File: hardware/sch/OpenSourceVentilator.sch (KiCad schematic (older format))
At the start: 16 parts, among them J101 Conn_TM1638_Disp, J102 24V Barrel Jack, J103 Conn_Stepper_Motor, J104 Conn_Beeper, J105 Conn_A4988_Stepper, J106 Conn_Motor_PWR, J107 Conn_Nano_PWR, J108 Conn_Nano_Pwr, J109 Conn_BME280, J110 Conn_A4988_Stepper, J111 Conn_Motor_PWR

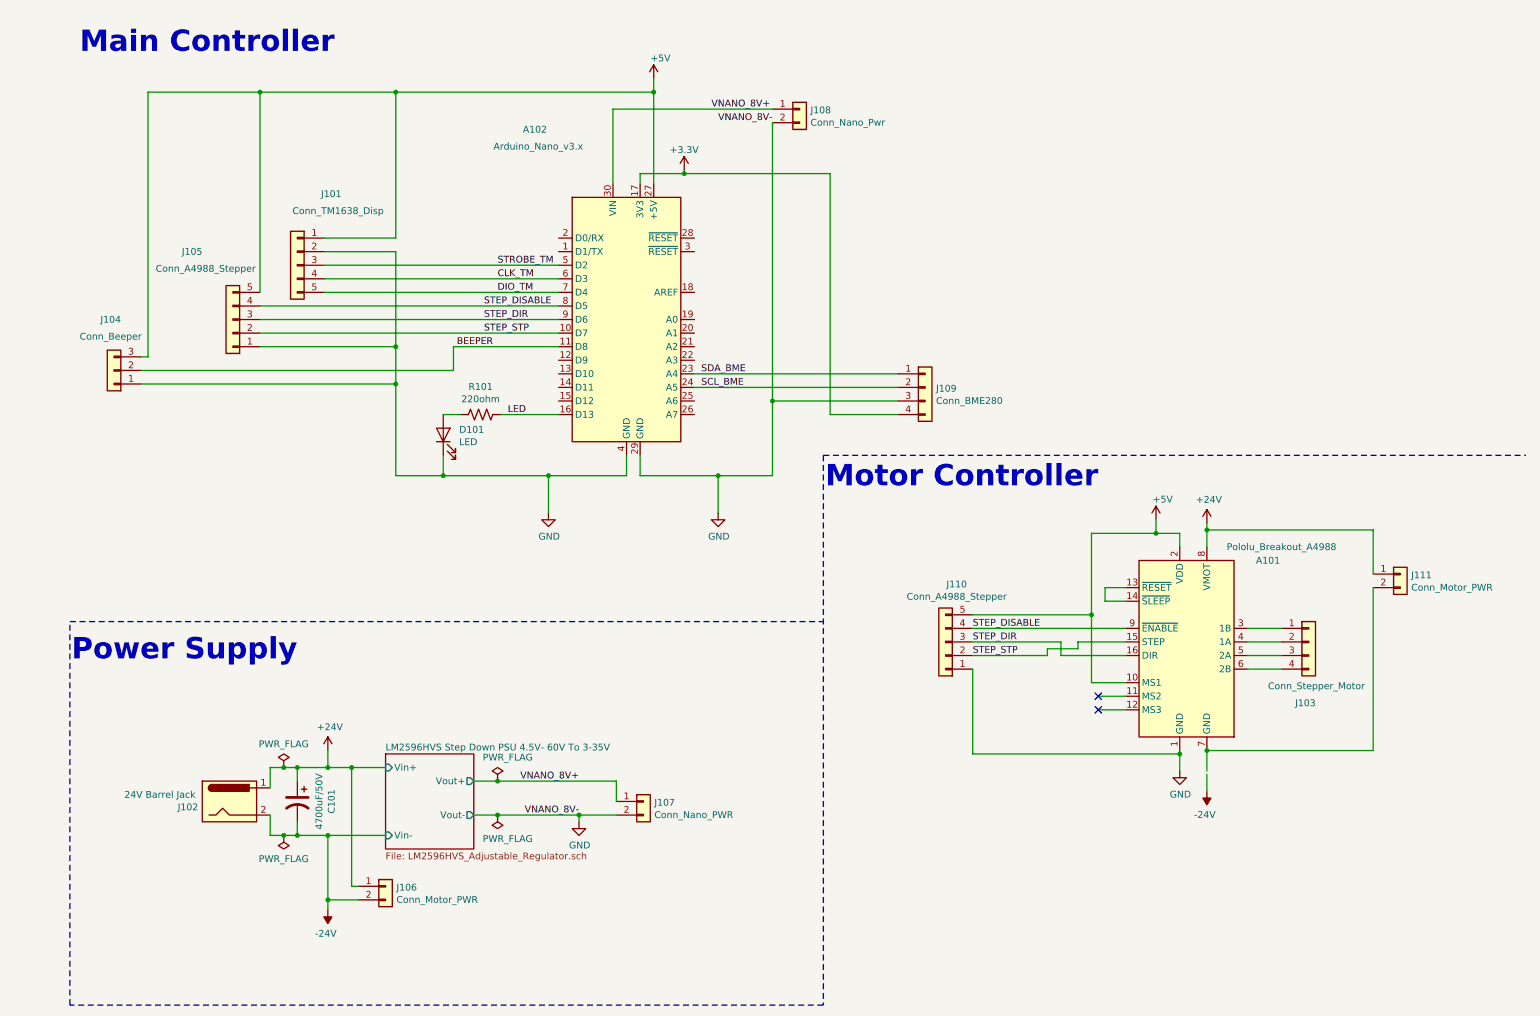
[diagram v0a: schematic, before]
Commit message: Added atmega328 datasheet Added arduino datasheet Added pwr jack voltage sense circuit, additional BME280 connector, decoupling caps on nano power input and a4988 power input, changed label refs Added I2C pullups, power switch, alarm latch circuit, limit switch
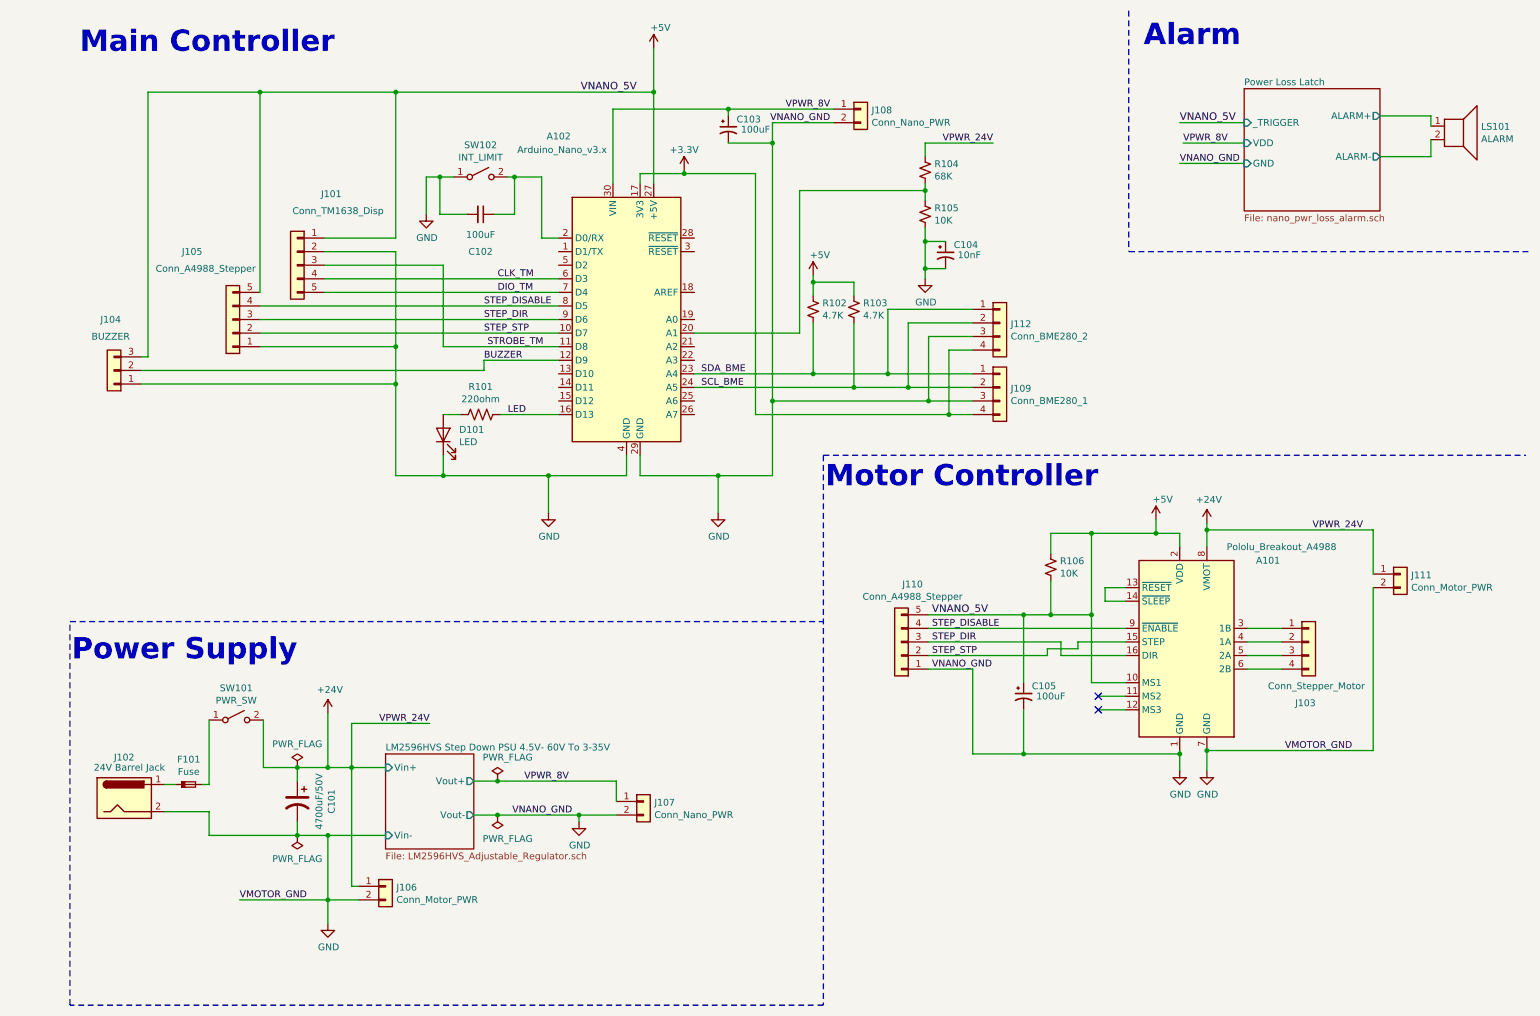
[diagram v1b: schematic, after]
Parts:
- added C102: 100uF, symbol Device:C_Small
- added C103, C105: 100uF, symbol Device:CP1_Small
- added C104: 10nF, symbol Device:CP1_Small
- added F101: Fuse, symbol Device:Fuse_Polarized_Small
- added J112: Conn_BME280_2, symbol Connector_Generic:Conn_01x04
- added LS101: ALARM, symbol Device:Speaker
- added R102, R103: 4.7K, symbol Device:R_Small_US
- added R104: 68K, symbol Device:R_Small_US
- added R105, R106: 10K, symbol Device:R_Small_US
- added SW101: PWR_SW, symbol Switch:SW_SPST
- added SW102: INT_LIMIT, symbol Switch:SW_SPST
- J104: value Conn_Beeper -> BUZZER
- J108: value Conn_Nano_Pwr -> Conn_Nano_PWR
- J109: value Conn_BME280 -> Conn_BME280_1
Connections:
- net -24V is gone; now on net GND: C101.2, J102.2, J106.2 (Pin_2)
- net +24V: now also R104.2, SW101.2 (B); no longer J102.1
- net +3V3: now also J112.4 (Pin_4)
- net +5V: now also C105.1, R102.2, R103.2, R106.1, R106.2
- net GND: now also A101.7 (GND), J111.2 (Pin_2), C102.2, C103.2, C104.1, C104.2, C105.2, J112.3 (Pin_3), R105.1, SW102.1 (A)
- net SCL_BME: now also J112.2 (Pin_2), R103.1
- net SDA_BME: now also J112.1 (Pin_1), R102.1
- net STROBE_TM: now also A102.11 (D8); no longer A102.5 (D2)
- net BUZZER: now reaches A102.12 (D9)
- net BUZZER: now also J104.2 (Pin_2)
- net at A102.2 (D0/RX): now also C102.1, SW102.2 (B)
- net at A102.20 (A1): now also R104.1, R105.2
- removed net BEEPER: A102.11 (D8), J104.2 (Pin_2)
- net VNANO_8V+ renamed VPWR_8V
- net VPWR_8V: now also C103.1
- new net: F101.2, SW101.1 (A)
- new net: F101.1, J102.1
- new net Power Loss Latch/ALARM+: LS101.1
- new net Power Loss Latch/ALARM-: LS101.2
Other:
- note added: "Alarm"
- moved on the sheet: J102, J108, J109, J110

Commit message: -Moved C104 to junction R104/R105 -Change I2C to 10K resistors -Moved R307 to VDD and G-Q304/C-Q303 junction -Updated K301 relay with G6EU -Remove D101 - LED -Added Analog User Controls (Buttons + PEEP/RR/TV Controls) -Added LCD PCF8574 module to I2C (Assume GND, VCC, SDA, SCL pin sequence) -Added schematic notes not to include alarm for controller prototyping.
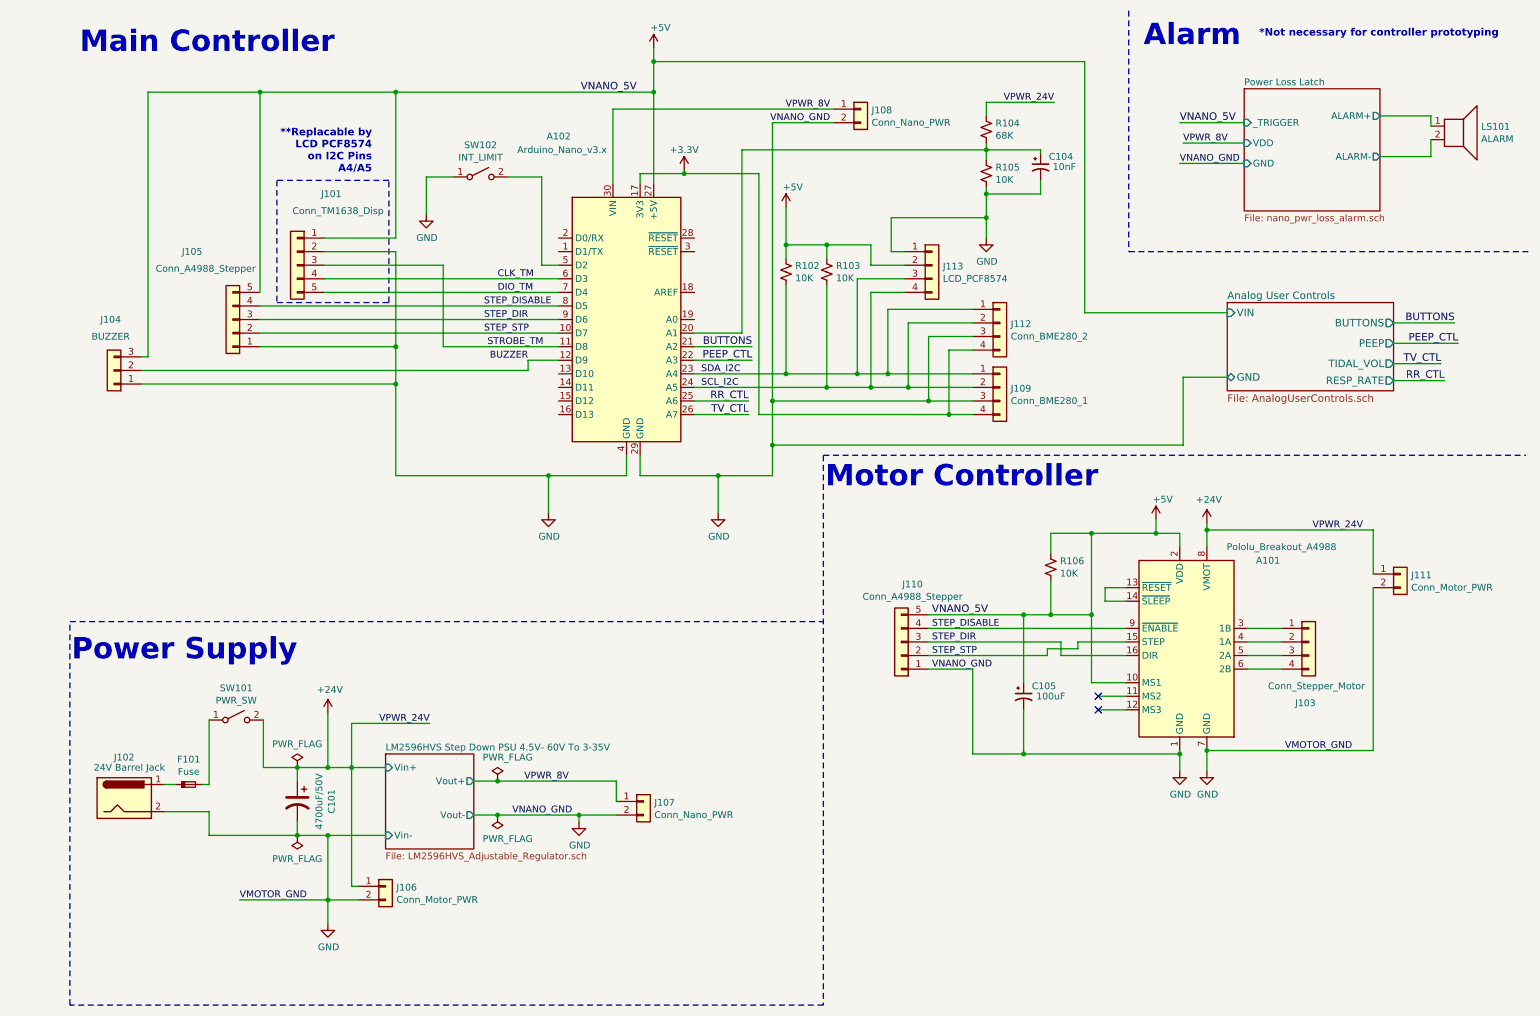
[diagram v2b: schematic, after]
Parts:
- removed C102: 100uF, symbol Device:C_Small
- removed C103: 100uF, symbol Device:CP1_Small
- removed D101: LED, symbol Device:LED
- removed R101: 220ohm, symbol Device:R_US
- added J113: LCD_PCF8574, symbol Connector_Generic:Conn_01x04
- R102, R103: value 4.7K -> 10K
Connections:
- net +5V: now also J113.2 (Pin_2)
- net GND: now also J113.1 (Pin_1); no longer C104.1
- net at A102.2 (D0/RX): no longer SW102.2 (B)
- net at A102.20 (A1), R104.1, R105.2: now also C104.1
- net BUTTONS: now reaches A102.21 (A2)
- net PEEP_CTL: now reaches A102.22 (A3)
- net RR_CTL: now reaches A102.25 (A6)
- net TV_CTL: now reaches A102.26 (A7)
- net at A102.5 (D2): now also SW102.2 (B)
- net LED: no longer names the net of A102.16 (D13)
- net SCL_BME renamed SCL_I2C
- net SCL_I2C: now also J113.4 (Pin_4)
- net SDA_BME renamed SDA_I2C
- net SDA_I2C: now also J113.3 (Pin_3)
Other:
- note added: "**Replacable by\nLCD PCF8574 \non I2C Pins\nA4/A5"
- note added: "*Not necessary for controller prototyping"
- moved on the sheet: C104, R102, R103, R104, R105

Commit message: Added sch changes? not sure what
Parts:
- A102: value Arduino_Nano_v3.x -> ARDUINO_NANO
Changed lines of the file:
@@
 P 4575 2750
 F 0 "A102" H 4075 4100 50  0000 C CNN
-F 1 "Arduino_Nano_v3.x" H 4100 4000 50  0000 C CNN
+F 1 "ARDUINO_NANO" H 4100 4000 50  0000 C CNN
 F 2 "Module:Arduino_Nano" H 4575 2750 50  0001 C CIN
 F 3 "http://www.mouser.com/pdfdocs/Gravitech_Arduino_Nano3_0.pdf" H 4575 2750 50  0001 C CNN
